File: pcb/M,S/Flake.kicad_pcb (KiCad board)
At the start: 2 copper layers, 139.3 x 95 mm, 55 parts, among them SW1 SW_Push, SW10 SW_Push, SW11 SW_Push, SW12 SW_Push, SW13 SW_Push, SW14 SW_Push, SW15 SW_Push, SW16 SW_Push, SW17 SW_Push, SW18 SW_Push, SW19 SW_Push, SW2 SW_Push, SW20 SW_Push, SW21 SW_Push, SW22 SW_Push, SW23 SW_Push, SW3 SW_Push, SW4 SW_Push, SW5 SW_Push, SW6 SW_Push, SW7 SW_Push, SW8 SW_Push, SW9 SW_Push, U1 XIAO-nRF52840-SMD

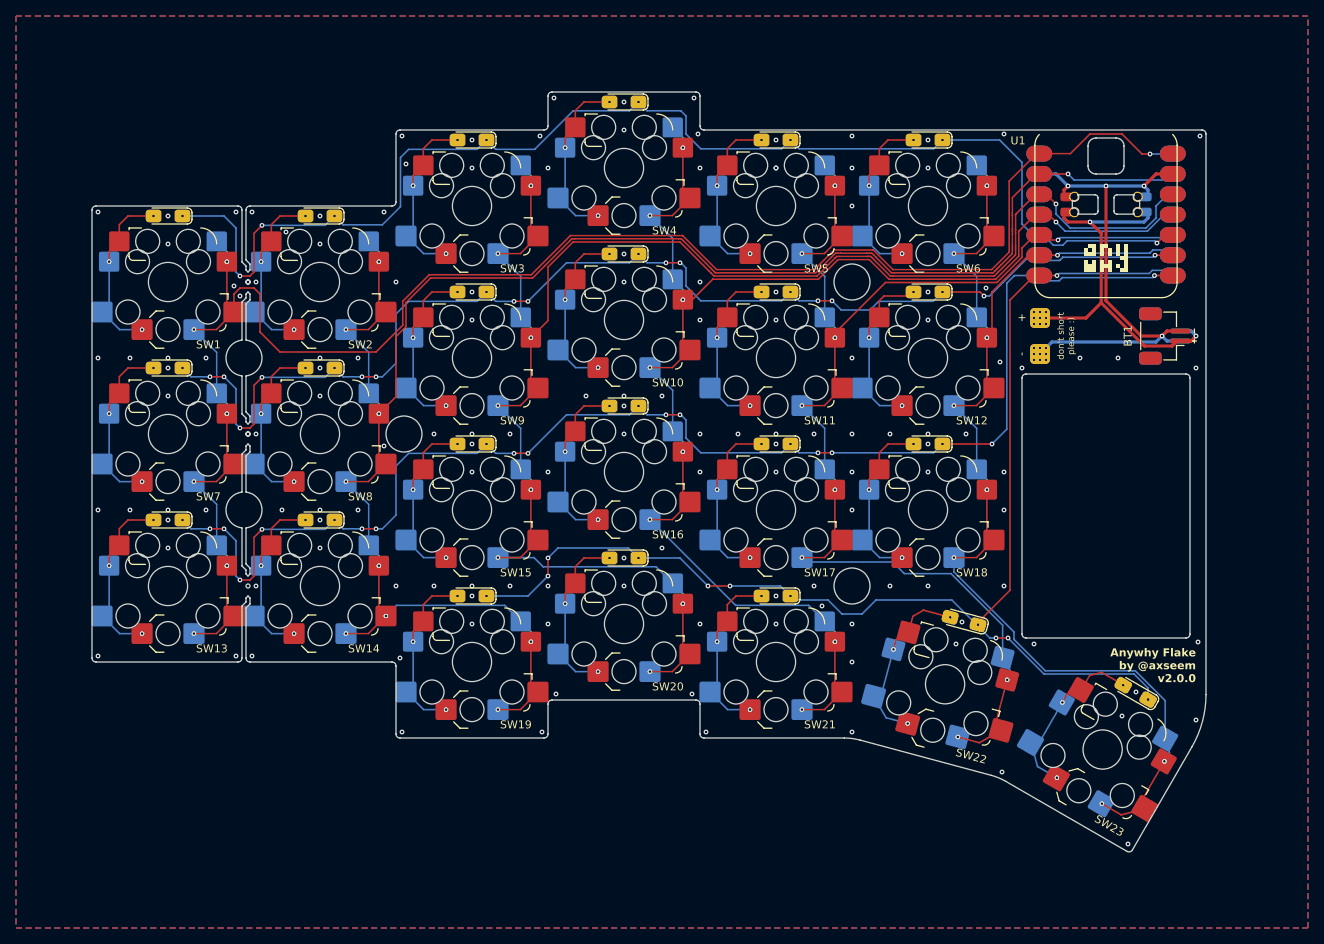
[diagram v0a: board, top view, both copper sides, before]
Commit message: fix(pcb): v2.0.1 boards with 1mm corner cuts and M,S reroute
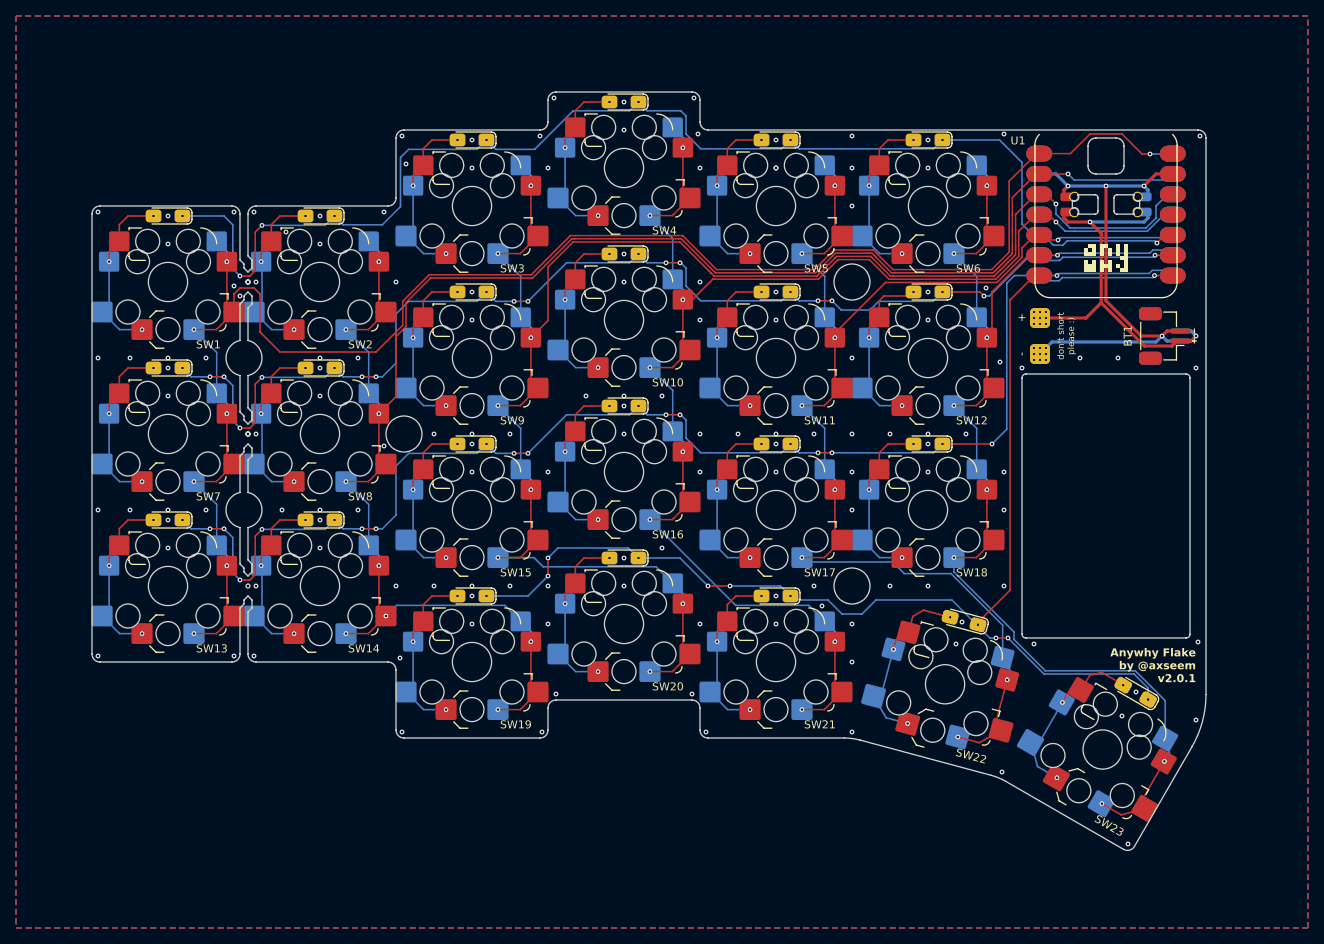
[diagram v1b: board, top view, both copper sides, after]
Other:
- board size 139.3 x 95 mm -> 139.3 x 94.8 mm
- board text added: "Anywhy Flake by @axseem v2.0.1"
- board text removed: "Anywhy Flake by @axseem v2.0.0"
